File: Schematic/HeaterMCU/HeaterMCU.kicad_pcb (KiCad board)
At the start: 2 copper layers, 100 x 35 mm, 48 parts, among them J1 MCU_Interface, J2 Firmware, SW1 RESET, U1 AMS1117-3.3, U2 Display_IPS_1.3_SPI, U3 ATMEGA328P-AU, U4 INA219AIDCNR, U5 TPS54302, Y1 16MHz

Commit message: Minor layout changes
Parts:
- added G***: LOGO, Graphics:retronics_logo_24mm, B.Cu at (73.6, 58.8)
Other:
- board text added: "JLCJLCJLCJLC"
- board text added: "µTracer Heater MCU 22_43_0120 Bjørner Sandom"

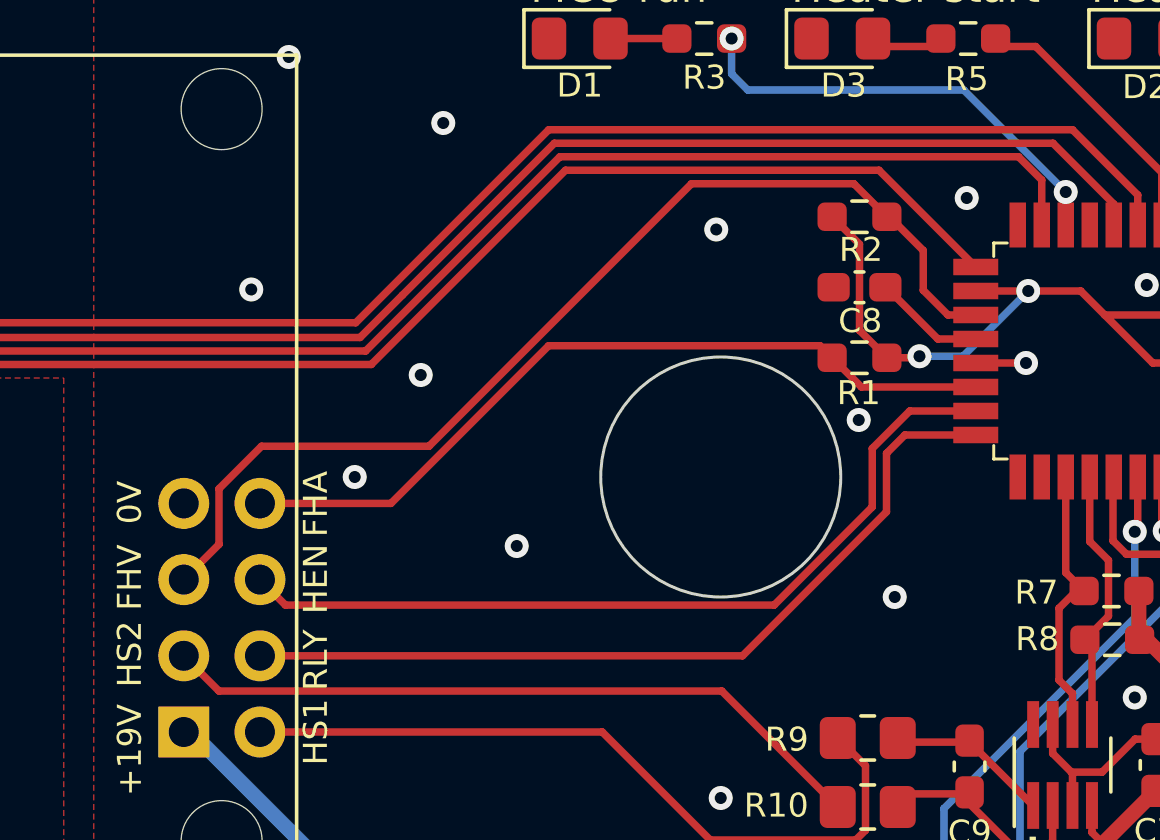
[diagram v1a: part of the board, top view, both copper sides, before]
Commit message: Larger mounting hole for rotary switch
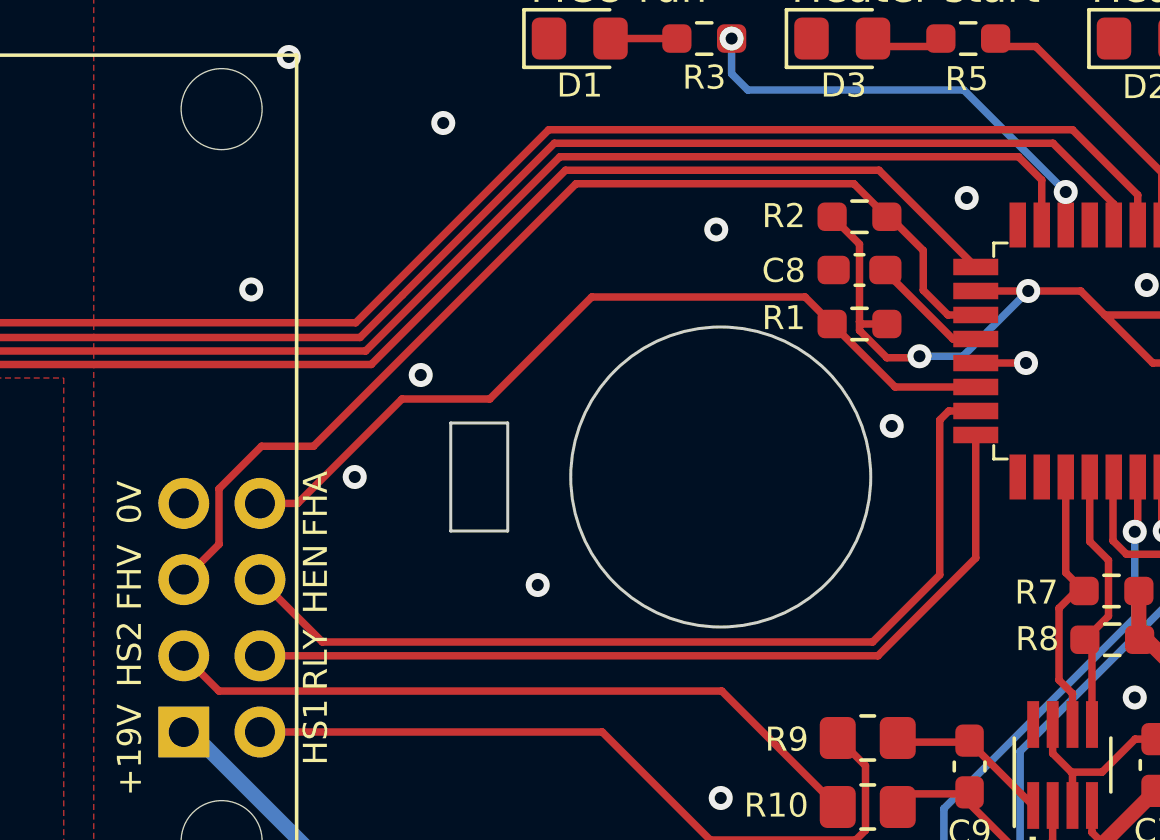
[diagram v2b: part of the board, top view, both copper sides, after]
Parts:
- moved R1 1.12 mm to (114.5, 57.4)
- moved C8 0.57 mm to (114.5, 55.6)
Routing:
- net Heater_EN: track 28.0 -> 30.9 mm
- net FlagMBHeaterActive: track 26.6 -> 28.0 mm
- net RLY_CTRL: track 28.1 -> 29.3 mm
- net +5V: track 138.9 -> 139.8 mm
- net GNDPWR: vias 32 -> 31
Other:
- outline, holes or cut-outs redrawn
- board text added: "µTracer Heater MCU 22_43_0120B Bjørner Sandom"
- board text removed: "µTracer Heater MCU 22_43_0120 Bjørner Sandom"

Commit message: Updated annotation
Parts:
- renumbered C1 to C301, C3 to C302, C4 to C303, C5 to C304, C6 to C305, C7 to C306, C8 to C307, C9 to C308, C10 to C309, C11 to C310, C12 to C311, C13 to C312, C14 to C313, C15 to C314, C16 to C315, D1 to D301, D2 to D302, D3 to D303, D4 to D304, FB1 to FB301, H1 to H301, H2 to H302, H3 to H303, H4 to H304, J1 to J301, J2 to J302, L1 to L301, R1 to R301, R2 to R302, R3 to R303, R4 to R304, R5 to R305, R6 to R306, R7 to R307, R8 to R308, R9 to R309, R10 to R310, R11 to R311, R12 to R312, R13 to R313, R14 to R314, SW1 to SW301, U1 to U301, U2 to U302, U3 to U303, U4 to U304, U5 to U305, Y1 to Y301
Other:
- outline, holes or cut-outs redrawn

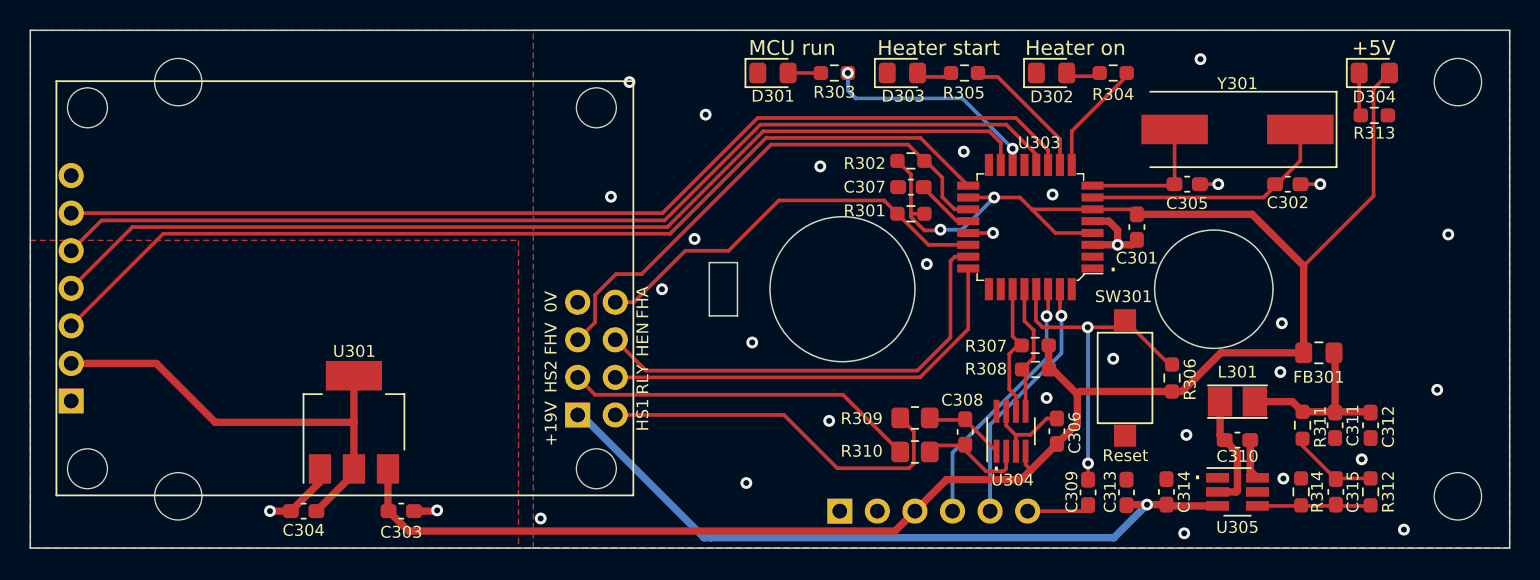
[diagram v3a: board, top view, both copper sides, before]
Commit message: MCU Board adapted for 3.3V operation
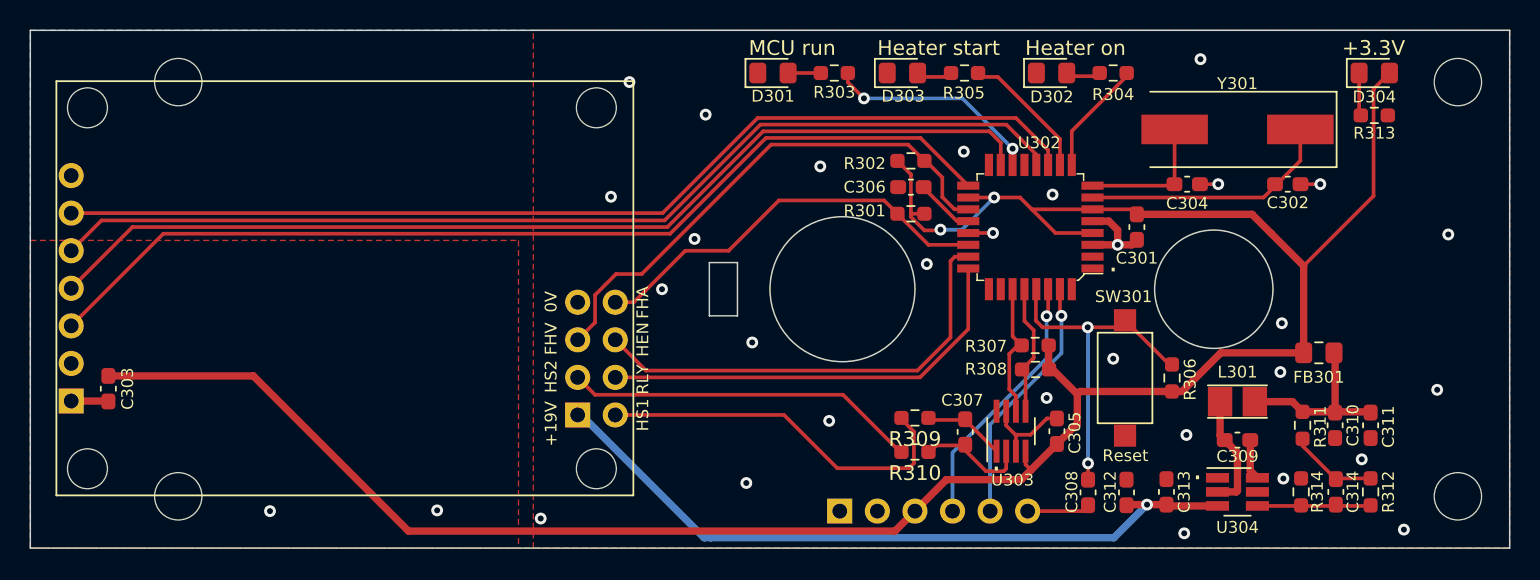
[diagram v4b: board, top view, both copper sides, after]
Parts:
- removed the C303 at (80.1, 77.5)
- removed the U301 at (76.9, 71.5)
- C303: renamed from C304; value 100nF -> 1µF
- C310: renamed from C311; value 22µF 25V -> 22µF 10V
- C312: renamed from C313; value 10µF 50V -> 10µF 35V
- R309, R310: footprint Resistor_SMD:R_0805_2012Metric_Pad1.20x1.40mm_HandSolder -> Resistor_SMD:R_0603_1608Metric_Pad0.98x0.95mm_HandSolder
- R314: value 13.3kΩ -> 22kΩ
- moved C303 15.6 mm to (60.3, 69.2), turned to 90 degrees
- renumbered C305 to C304, C306 to C305, C307 to C306, C308 to C307, C309 to C308, C310 to C309, C312 to C311, C314 to C313, C315 to C314, U302 to U301, U303 to U302, U304 to U303, U305 to U304
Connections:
- C301 pad 2: +5V -> +3V3
- C303 pad 2: Net-(C304-Pad2) -> +3V3
- C305 pad 2: +5V -> +3V3
- D304 pad 2: +5V -> +3V3
- FB301 pad 2: +5V -> +3V3
- J302 pad 3: +5V -> +3V3
- R301 pad 1: +5V -> +3V3
- R302 pad 1: +5V -> +3V3
- R306 pad 1: +5V -> +3V3
- R307 pad 2: +5V -> +3V3
- R308 pad 1: +5V -> +3V3
- U301 pad 2: Net-(C304-Pad2) -> +3V3
- U302 pad 18: +5V -> +3V3
- U302 pad 4: +5V -> +3V3
- U302 pad 6: +5V -> +3V3
- U303 pad 4: +5V -> +3V3
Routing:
- net +3V3: track 0.00 -> 159.7 mm, vias 0 -> 2
- net +5V: track 139.8 -> 0.00 mm, vias 2 -> 0
- net Net-(C304-Pad2): track 31.3 -> 0.00 mm
- net GNDPWR: track 23.2 -> 19.1 mm
- added copper zone on F.Cu, net +3V3
- removed copper zone on F.Cu, net Net-(C304-Pad2)
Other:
- board text added: "+3.3V"
- board text added: "µTracer Heater MCU 22_43_0120C Bjørner Sandom"
- board text removed: "µTracer Heater MCU 22_43_0120B Bjørner Sandom"

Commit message: Optocouplers moved to from PSU to MCU board
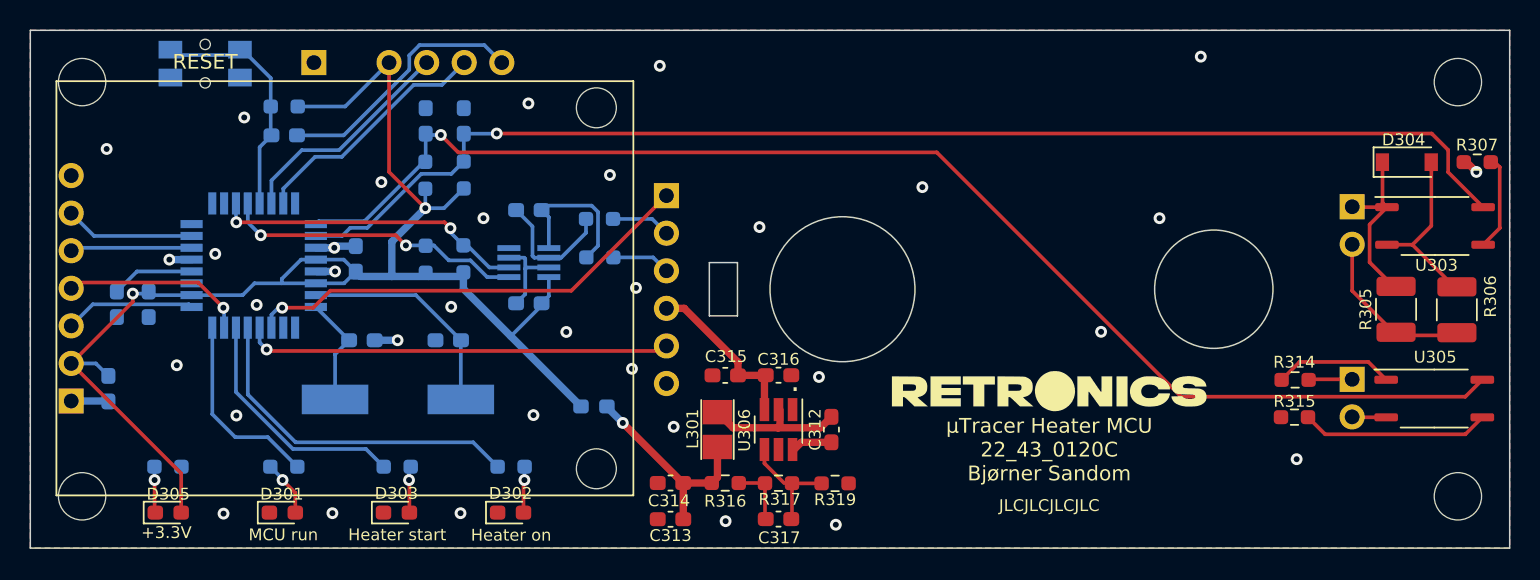
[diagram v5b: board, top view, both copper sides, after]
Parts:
- added C303: 100nF, Capacitor_SMD:C_0603_1608Metric_Pad1.08x0.95mm_HandSolder, B.Cu at (63.0, 63.5)
- added C308: 220nF, Capacitor_SMD:C_0603_1608Metric_Pad1.08x0.95mm_HandSolder, B.Cu at (84.3, 51.1)
- added C311: 220nF, Capacitor_SMD:C_0603_1608Metric_Pad1.08x0.95mm_HandSolder, B.Cu at (81.7, 51.1)
- added D304: 1N4148W, Diode_SMD:D_SOD-123, F.Cu at (148.0, 53.9)
- added J302: Heater Control, Connector_PinSocket_2.54mm:PinSocket_1x02_P2.54mm_Horizontal, B.Cu at (144.4, 56.9)
- added J303: High voltage warning, Connector_PinSocket_2.54mm:PinSocket_1x02_P2.54mm_Horizontal, B.Cu at (144.3, 68.6)
- added R305: 3.9kΩ 1/2W, Resistor_SMD:R_1210_3225Metric_Pad1.30x2.65mm_HandSolder, F.Cu at (147.3, 63.9)
- added R306: 3.9kΩ 1/2W, Resistor_SMD:R_1210_3225Metric_Pad1.30x2.65mm_HandSolder, F.Cu at (151.4, 63.9)
- added R307: 220Ω, Resistor_SMD:R_0603_1608Metric_Pad0.98x0.95mm_HandSolder, F.Cu at (152.8, 53.9)
- added R314: 220Ω, Resistor_SMD:R_0603_1608Metric_Pad0.98x0.95mm_HandSolder, F.Cu at (140.5, 68.6)
- added R315: 220Ω, Resistor_SMD:R_0603_1608Metric_Pad0.98x0.95mm_HandSolder, F.Cu at (140.5, 71.2)
- added U303: TLP185, Package_SO:SOIC-4_4.55x3.7mm_P2.54mm, F.Cu at (150.0, 58.2)
- added U305: TLP185, Package_SO:SOIC-4_4.55x3.7mm_P2.54mm, F.Cu at (149.9, 69.9)
- C301: renamed from C303; moved to B.Cu
- C302: renamed from C301; moved to B.Cu
- C304: renamed from C302; moved to B.Cu
- C305: renamed from C304; moved to B.Cu
- C306: renamed from C305; moved to B.Cu
- C307: renamed from C306; moved to B.Cu
- C309: renamed from C307; moved to B.Cu
- C310: renamed from C308; moved to B.Cu
- D301, D302, D303: footprint LED_SMD:LED_0805_2012Metric_Pad1.15x1.40mm_HandSolder -> LED_SMD:LED_0603_1608Metric_Pad1.05x0.95mm_HandSolder
- D305: renamed from D304; footprint LED_SMD:LED_0805_2012Metric_Pad1.15x1.40mm_HandSolder -> LED_SMD:LED_0603_1608Metric_Pad1.05x0.95mm_HandSolder
- FB301: footprint Inductor_SMD:L_0805_2012Metric_Pad1.15x1.40mm_HandSolder -> Inductor_SMD:L_0603_1608Metric_Pad1.05x0.95mm_HandSolder; moved to B.Cu
- G***: moved to F.Cu
- J301: value MCU_Interface -> Conn_01x06; footprint Connector_PinHeader_2.54mm:PinHeader_2x04_P2.54mm_Vertical -> Connector_PinSocket_2.54mm:PinSocket_1x06_P2.54mm_Vertical
- R301: renamed from R303; moved to B.Cu
- R302: renamed from R304; moved to B.Cu
- R303: renamed from R305; moved to B.Cu
- R304: renamed from R301; moved to B.Cu
- R308: renamed from R306; moved to B.Cu
- R309: renamed from R307; moved to B.Cu
- R310: renamed from R308; moved to B.Cu
- R311: renamed from R309; moved to B.Cu
- R312: renamed from R302; moved to B.Cu
- R313: renamed from R310; moved to B.Cu
- R318: renamed from R313; moved to B.Cu
- SW301: footprint Button_Switch_SMD:SW_SPST_CK_RS282G05A3 -> myDevices:Tactile_sw_SMD_side_01; moved to B.Cu
- U302: moved to B.Cu
- U304: renamed from U303; moved to B.Cu
- Y301: value 16MHz -> 8MHz; moved to B.Cu
- moved D305 86.8 mm to (64.3, 77.6)
- moved R318 84.9 mm to (64.3, 74.5)
- moved SW301 65.8 mm to (66.8, 47.0), turned to 0 degrees
- moved R308 62.8 mm to (72.2, 50.1), turned to 180 degrees
- moved Y301 59.6 mm to (79.8, 70.0)
- moved C310 59.5 mm to (72.2, 52.1), turned to 180 degrees
- moved C304 57.7 mm to (83.2, 66.0), turned to 180 degrees
- moved C305 56.8 mm to (77.4, 66.0)
- moved C307 54.3 mm to (60.9, 63.5), turned to 90 degrees
- moved C302 52.8 mm to (77.0, 60.5), turned to -90 degrees
- moved U302 52.6 mm to (70.1, 60.9)
- moved G*** 51.4 mm to (123.9, 69.3), turned to 0 degrees
- moved FB301 49.1 mm to (93.1, 70.4)
- moved R302 48.6 mm to (87.5, 74.5), turned to 180 degrees
- moved C314 47.5 mm to (98.3, 75.6), turned to 0 degrees
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- renumbered C309 to C312, C310 to C313, C311 to C314, C312 to C315, C313 to C316, C314 to C317, J302 to J304, R311 to R316, R312 to R317, R314 to R319, U304 to U306
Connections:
- J301 pad 1: VDC -> RLY_CTRL
- J301 pad 2: HeaterSense1 -> HeaterSense2
- J301 pad 3: HeaterSense2 -> HeaterSense1
- J301 pad 4: RLY_CTRL -> VDC
- J301 pad 5: FlagHighVoltage -> Heater_EN
- J301 pad 6: Heater_EN -> GNDPWR
- U302 pad 1: unconnected-(U302-Pad1) -> FlagHighVoltage
- U302 pad 10: LED_Heater_Start -> unconnected-(U302-Pad10)
- U302 pad 11: Disp_DC -> RLY_CTRL
- U302 pad 12: Disp_RES -> Heater_EN
- U302 pad 13: unconnected-(U302-Pad13) -> LED_Heater_ON
- U302 pad 14: LED_MCU_ON -> LED_Heater_Start
- U302 pad 16: unconnected-(U302-Pad16) -> LED_MCU_ON
- U302 pad 19: FlagHighVoltage -> unconnected-(U302-Pad19)
- U302 pad 2: unconnected-(U302-Pad2) -> FlagMBHeaterActive
- U302 pad 22: FlagMBHeaterActive -> Disp_RES
- U302 pad 23: Heater_EN -> Disp_DC
- U302 pad 24: RLY_CTRL -> unconnected-(U302-Pad24)
- U302 pad 9: LED_Heater_ON -> unconnected-(U302-Pad9)
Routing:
- net Disp_DC: track 71.0 -> 8.78 mm
- net Disp_RES: track 70.3 -> 8.22 mm
- net +3V3: track 159.7 -> 97.6 mm
- net Disp_SCL: track 67.2 -> 8.82 mm
- net FlagMBHeaterActive: track 28.0 -> 85.8 mm, vias 0 -> 1
- net Disp_SDA: track 69.1 -> 12.5 mm, vias 0 -> 1
- net FlagHighVoltage: track 35.5 -> 90.4 mm, vias 0 -> 1
- net VDC: track 49.1 -> 11.5 mm, vias 1 -> 0
- net HeaterSense1: track 25.3 -> 3.96 mm
- net HeaterSense2: track 23.9 -> 4.01 mm
- net LED_Heater_ON: track 7.54 -> 23.4 mm
- net Net-(C310-Pad1): track 4.25 -> 17.4 mm
- net Net-(R315-Pad2): track 0.00 -> 12.7 mm
- net Net-(D304-Pad1): track 0.00 -> 12.6 mm
- net Net-(D304-Pad2): track 0.00 -> 12.4 mm
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- removed copper zone on F.Cu, net +3V3
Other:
- board text added: "K A From MB HV LED"
- board text added: "R L From MB heater"
- board text added: "RESET"
- board text removed: "+19V"
- board text removed: "+5V"
- board text removed: "0V"
- board text removed: "FHA"
- board text removed: "FHV"
- board text removed: "HEN"
- board text removed: "HS1"
- board text removed: "HS2"
- board text removed: "RLY"
- board text removed: "Reset"
- board text removed: "Rst"
- board text removed: "Rx"
- board text removed: "Tx"
